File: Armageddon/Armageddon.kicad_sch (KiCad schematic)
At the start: 22 parts, among them J1 XT60PW-M, J2 530470610, U1 TLVM13610RDFR

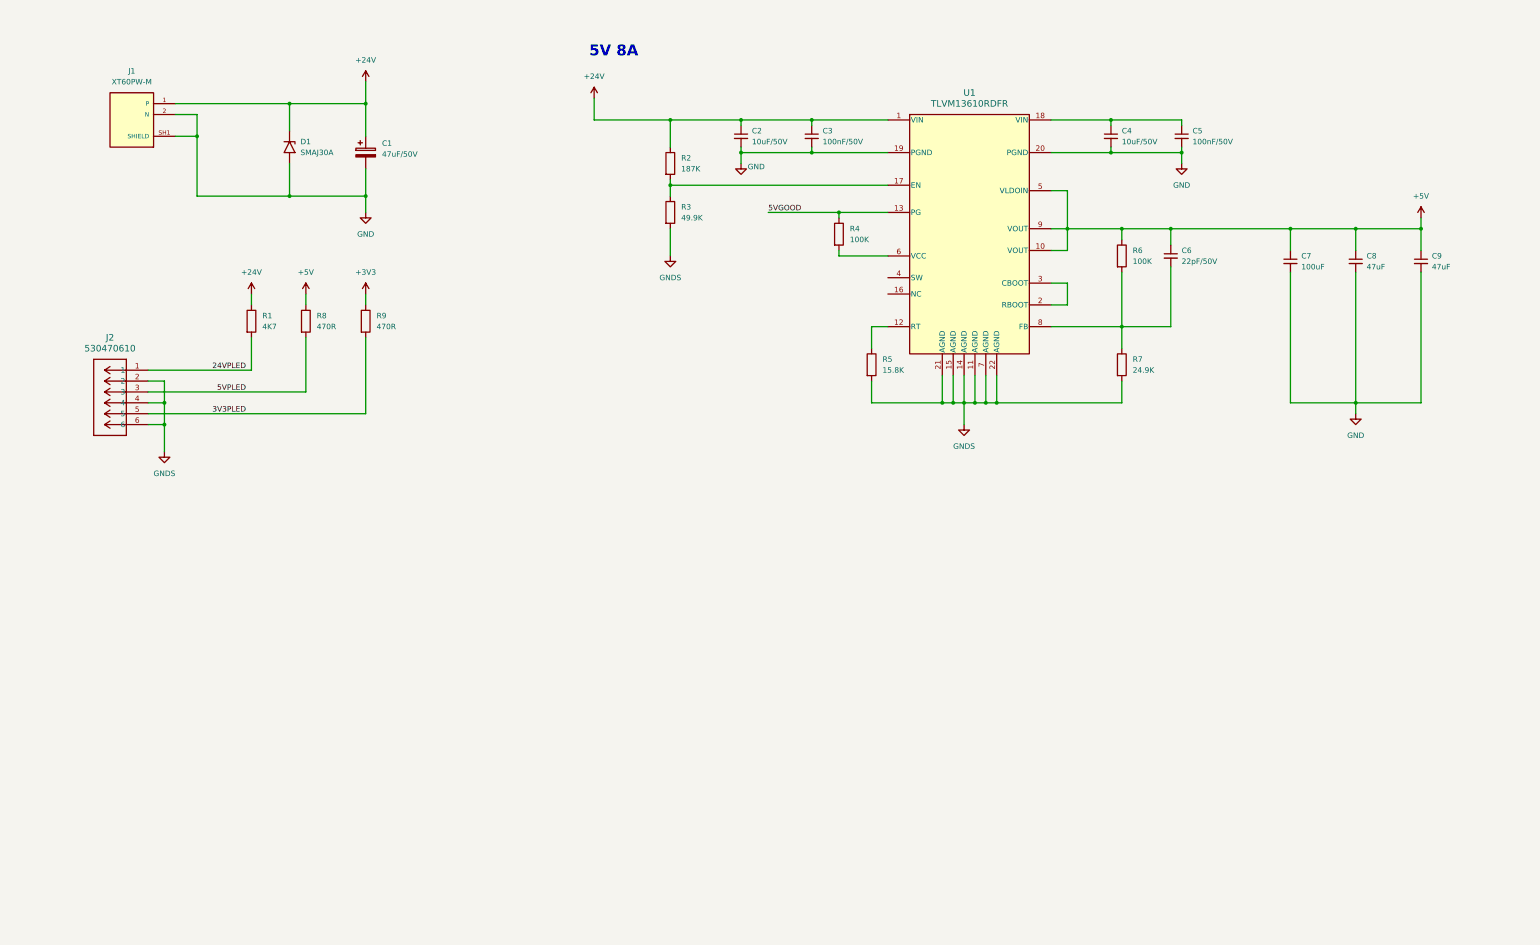
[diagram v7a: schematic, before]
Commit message: 3V3 Rail Added
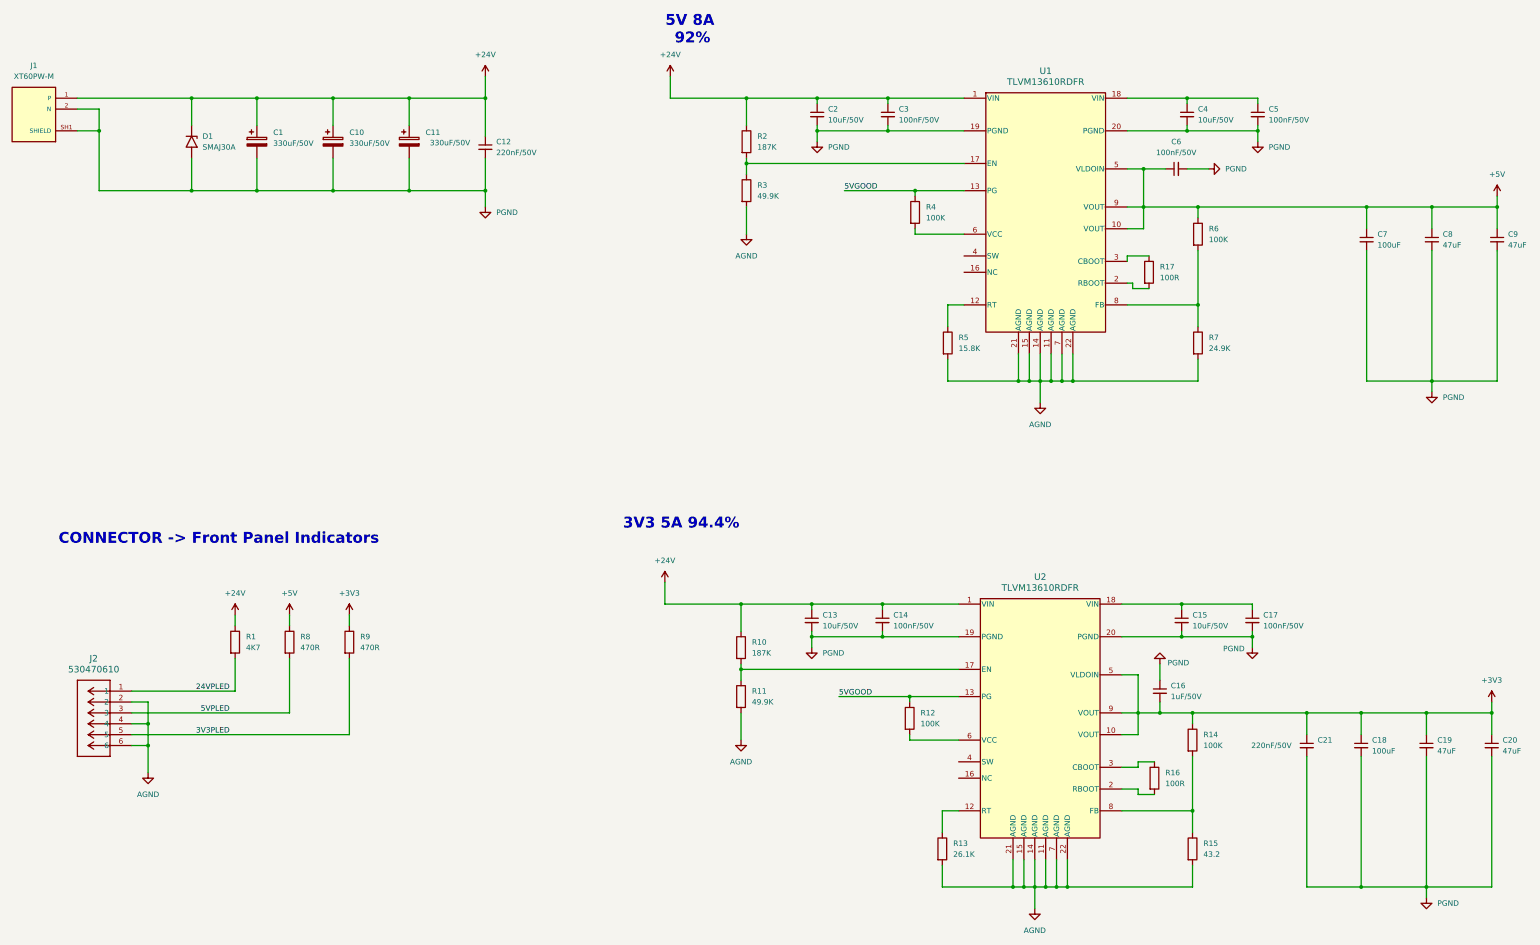
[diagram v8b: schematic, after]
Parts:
- added C10, C11: 330uF/50V, C_870135775004:WCAP-PTHT_10X12.5_DXL_, symbol Device:C_Polarized
- added C12, C21: 220nF/50V, Capacitor_SMD:C_0805_2012Metric_Pad1.18x1.45mm_HandSolder, symbol Device:C_Small
- added C13, C15: 10uF/50V, Capacitor_SMD:C_1206_3216Metric_Pad1.33x1.80mm_HandSolder, symbol Device:C_Small
- added C14, C17: 100nF/50V, Capacitor_SMD:C_0805_2012Metric_Pad1.18x1.45mm_HandSolder, symbol Device:C_Small
- added C16: 1uF/50V, Capacitor_SMD:C_0805_2012Metric_Pad1.18x1.45mm_HandSolder, symbol Device:C_Small
- added C18: 100uF, Capacitor_SMD:C_1206_3216Metric_Pad1.33x1.80mm_HandSolder, symbol Device:C_Small
- added C19, C20: 47uF, Capacitor_SMD:C_1206_3216Metric_Pad1.33x1.80mm_HandSolder, symbol Device:C_Small
- added R10: 187K, Resistor_SMD:R_0603_1608Metric_Pad0.98x0.95mm_HandSolder, symbol Device:R
- added R11: 49.9K, Resistor_SMD:R_0603_1608Metric_Pad0.98x0.95mm_HandSolder, symbol Device:R
- added R12, R14: 100K, Resistor_SMD:R_0603_1608Metric_Pad0.98x0.95mm_HandSolder, symbol Device:R
- added R13: 26.1K, Resistor_SMD:R_0603_1608Metric_Pad0.98x0.95mm_HandSolder, symbol Device:R
- added R15: 43.2, Resistor_SMD:R_0603_1608Metric_Pad0.98x0.95mm_HandSolder, symbol Device:R
- added R16, R17: 100R, Resistor_SMD:R_0603_1608Metric_Pad0.98x0.95mm_HandSolder, symbol Device:R
- added U2: TLVM13610RDFR, RDF0022A-MFG, symbol TVLM13610:TLVM13610RDFR
- C1: value 47uF/50V -> 330uF/50V
- C6: value 22pF/50V -> 100nF/50V
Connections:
- net +24V: now also C10.1, C11.1, C12.1, C13.1, C14.1, R10.1, U2.1 (VIN)
- net +3V3: now also C16.2, C18.1, C19.1, C20.1, C21.1, R14.1, U2.10 (VOUT), U2.5 (VLDOIN), U2.9 (VOUT)
- net 5VGOOD: now also R12.1, U2.13 (PG)
- net at R6.2, R7.1, U1.8 (FB): no longer C6.2
- net at U1.3 (CBOOT): now also R17.1; no longer U1.2 (RBOOT)
- net GND renamed PGND
- net PGND: now also C6.2, C10.2, C11.2, C12.2, C13.2, C14.2, C15.2, C16.1, C17.2, C18.2, C19.2, C20.2, C21.2, U2.19 (PGND), U2.20 (PGND)
- net GNDS renamed AGND
- net AGND: now also R11.2, R13.2, R15.2, U2.11 (AGND), U2.14 (AGND), U2.15 (AGND), U2.21 (AGND), U2.22 (AGND), U2.7 (AGND)
- new net: R17.2, U1.2 (RBOOT)
- new net: R12.2, U2.6 (VCC)
- new net: R16.1, U2.3 (CBOOT)
- new net: R16.2, U2.2 (RBOOT)
- new net: C15.1, C17.1, U2.18 (VIN)
- new net: R13.1, U2.12 (RT)
- new net: R10.2, R11.1, U2.17 (EN)
- new net: R14.2, R15.1, U2.8 (FB)
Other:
- note added: "3V3 5A 94.4%"
- note added: "5V 8A 92%"
- note added: "CONNECTOR -> Front Panel Indicators"
- note removed: "5V 8A"
- moved on the sheet: C1, C2, C3, C4, C5, C7, C8, C9, D1, J1, J2, R1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
